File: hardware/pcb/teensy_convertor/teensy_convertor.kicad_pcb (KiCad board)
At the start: 2 copper layers, 76.2 x 101.6 mm, 52 parts, among them SW1 SW_Push, SW2 SW_Push, SW3 SW_Push, SW4 SW_Push, SW5 SW_Push, SW6 SW_Push, SW7 SW_Push, SW8 SW_Push, SW9 SW_Push, U1 Teensy-3.2

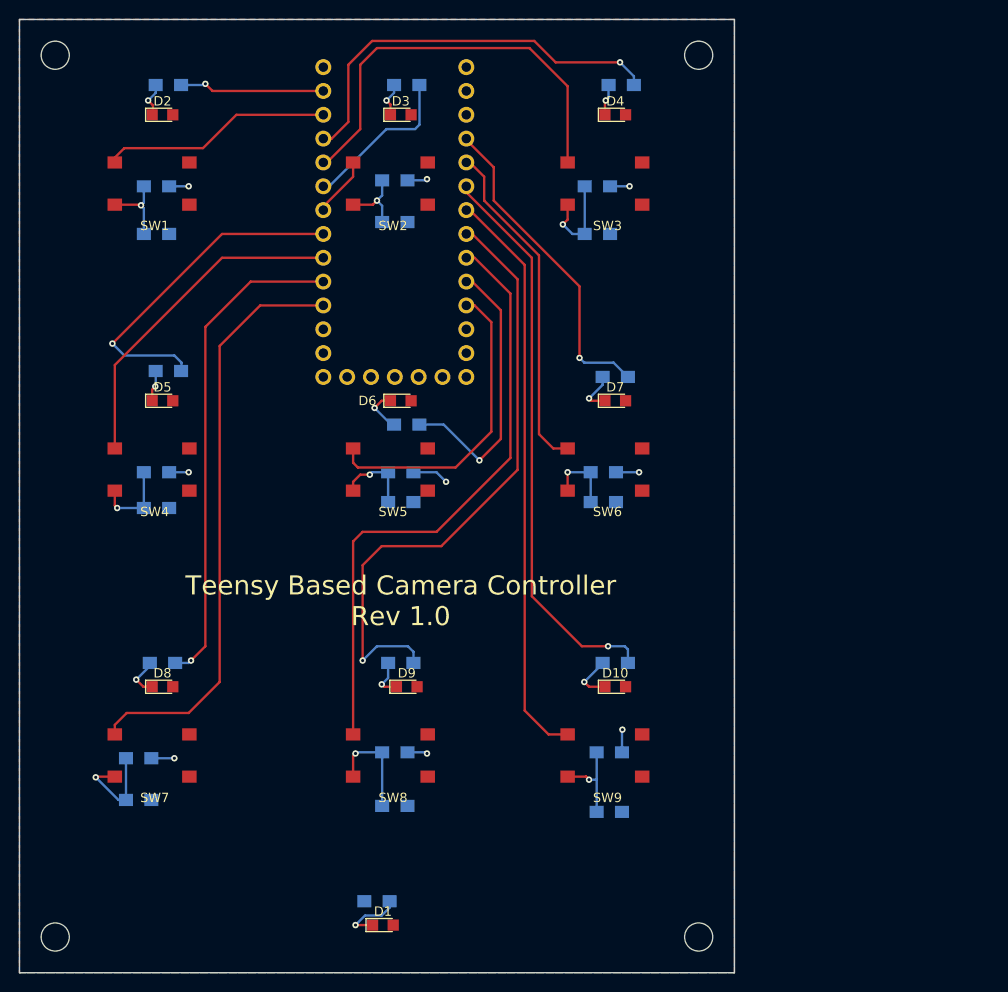
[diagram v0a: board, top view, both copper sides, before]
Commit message: Initial association and import into the layout tool
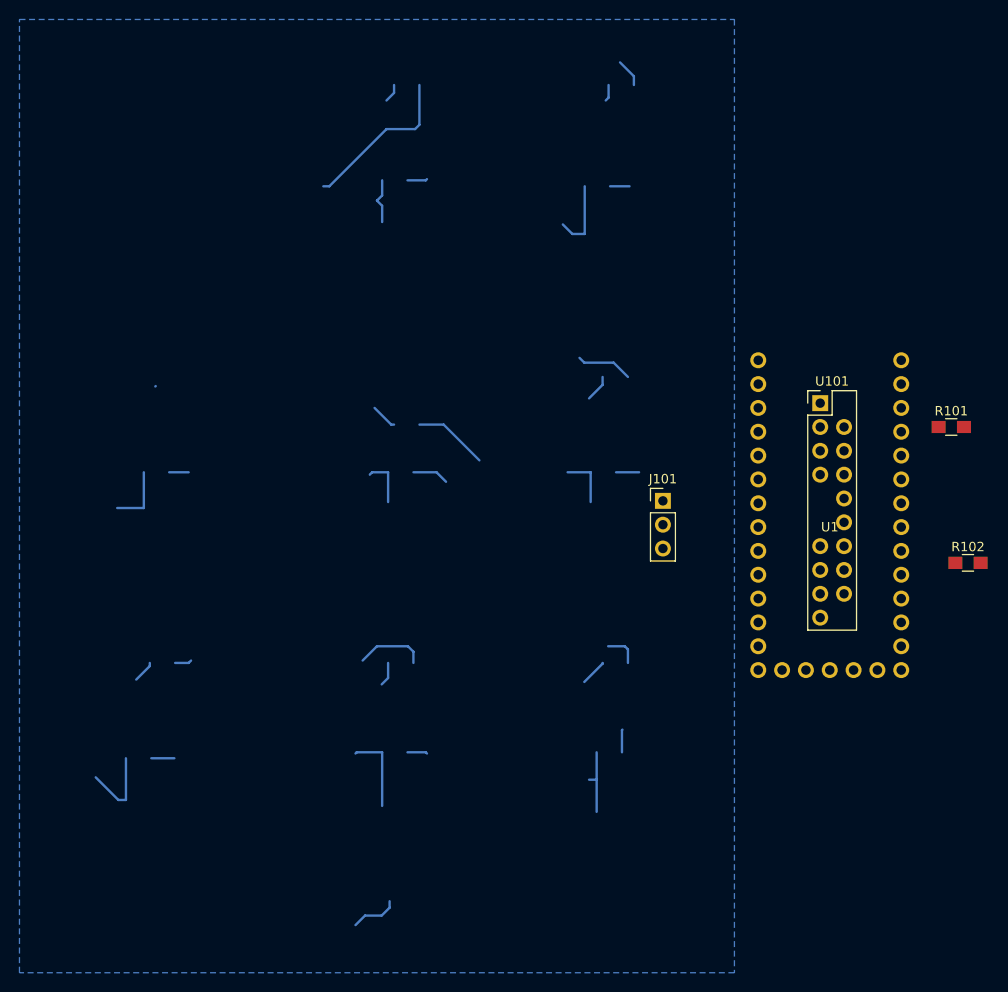
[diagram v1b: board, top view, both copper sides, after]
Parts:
- removed D1, D10, D2, D3, D4, D5, D6, D7, D8, D9: LED, LEDs:LED_0805
- removed R1, R10, R2, R3, R4, R5, R6, R7, R8, R9: 500, Resistors_SMD:R_0805_HandSoldering
- removed R11, R12, R13, R14, R15, R16, R17, R18, R19, R20, R21, R22, R23, R24, R25, R26, R27, R28: 1K, Resistors_SMD:R_0805_HandSoldering
- removed REF** (x4): MountingHole_3mm, Mounting_Holes:MountingHole_3mm
- removed SW1, SW2, SW3, SW4, SW5, SW6, SW7, SW8, SW9: SW_Push, Key:PTS645SK43SMTR92
- added J101: CONN_01X03, Pin_Headers:Pin_Header_Straight_1x03_Pitch2.54mm, F.Cu at (165.1, 91.9)
- added R101: 0, Resistors_SMD:R_0805_HandSoldering, F.Cu at (195.8, 84.1)
- added R102: 0, Resistors_SMD:R_0805_HandSoldering, F.Cu at (197.6, 98.6)
- added U101: MicroC_Header, micro_c_header:MicroC_Header_Pitch2.54mm, F.Cu at (181.9, 81.5)
- U1: footprint Key:Teensy-32 -> teensy_convertor:Teensy-32; moved to F.Cu
- moved U1 55.9 mm to (182.9, 92.2), turned to 0 degrees
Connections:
- U1 pad 0: /LED1 -> /TEENSY_RX
- U1 pad 1: /SW1 -> /TEENSY_TX
- U1 pad 10: Net-(U1-Pad10) -> /SPI_CS
- U1 pad 11: Net-(U1-Pad11) -> /SPI_MOSI
- U1 pad 12: Net-(U1-Pad12) -> /SPI_MISO
- U1 pad 13: Net-(U1-Pad13) -> /SPI_CLK
- U1 pad 14: Net-(U1-Pad14) -> /AIO0
- U1 pad 15: Net-(U1-Pad15) -> /AIO1
- U1 pad 16: /SW5 -> /AIO2
- U1 pad 17: /LED5 -> /AIO3
- U1 pad 18: /SW8 -> /I2C_SDAT
- U1 pad 19: /LED8 -> /I2C_SCLK
- U1 pad 2: /LED3 -> Net-(U1-Pad2)
- U1 pad 20: /SW9 -> Net-(U1-Pad20)
- U1 pad 21: /LED9 -> Net-(U1-Pad21)
- U1 pad 22: /SW6 -> Net-(U1-Pad22)
- U1 pad 23: /LED6 -> Net-(U1-Pad23)
- U1 pad 24: +3V3 -> /3.3V
- U1 pad 26: Net-(U1-Pad26) -> /5.0V
- U1 pad 27: GND -> /GND
- U1 pad 3: /SW3 -> Net-(U1-Pad3)
- U1 pad 4: /LED2 -> Net-(U1-Pad4)
- U1 pad 5: /SW2 -> Net-(U1-Pad5)
- U1 pad 6: /LED4 -> Net-(U1-Pad6)
- U1 pad 7: /SW4 -> Net-(U1-Pad7)
- U1 pad 8: /LED7 -> Net-(U1-Pad8)
- U1 pad 9: /SW7 -> Net-(U1-Pad9)
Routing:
- net (no net): track 0.00 -> 143.9 mm
- net /LED8: track 66.1 -> 0.00 mm, vias 1 -> 0
- net /SW8: track 65.5 -> 0.00 mm
- net /SW7: track 62.7 -> 0.00 mm
- net /SW9: track 61.8 -> 0.00 mm
- net /LED9: track 60.6 -> 0.00 mm, vias 1 -> 0
- net /LED7: track 52.6 -> 0.00 mm, vias 1 -> 0
- net /SW3: track 44.9 -> 0.00 mm
- net /LED3: track 43.5 -> 0.00 mm, vias 1 -> 0
- net /LED4: track 36.4 -> 0.00 mm, vias 1 -> 0
- net /SW6: track 36.1 -> 0.00 mm
- net /SW4: track 35.8 -> 0.00 mm
- net /LED6: track 34.4 -> 0.00 mm, vias 1 -> 0
- net /SW5: track 33.1 -> 0.00 mm
- net /LED5: track 29.9 -> 0.00 mm, vias 1 -> 0
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- removed copper zone on F.Cu, net +3V3
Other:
- board outline removed
- board text removed: "Teensy Based Camera Controller Rev 1.0"

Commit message: Initial layout
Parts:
- added REF**: 1pin, Connect:1pin, F.Cu at (173.5, 75.9)
- U1: moved to B.Cu
- moved J101 20.0 mm to (179.8, 78.5), turned to 90 degrees
- moved R102 19.5 mm to (185.2, 83.6), turned to 270 degrees
- moved R101 7.89 mm to (188.0, 83.6), turned to 90 degrees
- moved U101 3.78 mm to (179.1, 84.1)
- moved U1 0.36 mm to (182.6, 92.5), turned to 180 degrees
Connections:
- U1 pad 30: Net-(U1-Pad30) -> /GND
- U101 pad 7: Net-(U101-Pad7) -> Net-(R101-Pad1)
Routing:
- net (no net): track 143.9 -> 0.00 mm
- net /5.0V: track 0.00 -> 10.9 mm
- net Net-(J101-Pad2): track 0.00 -> 6.96 mm
- net /3.3V: track 0.00 -> 6.40 mm
- net /TEENSY_TX: track 0.00 -> 0.51 mm
- removed copper zone on B.Cu, net GND
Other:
- board outline added: 23.9 x 41.1 mm
- board text added: "3.3V"
- board text added: "5V"

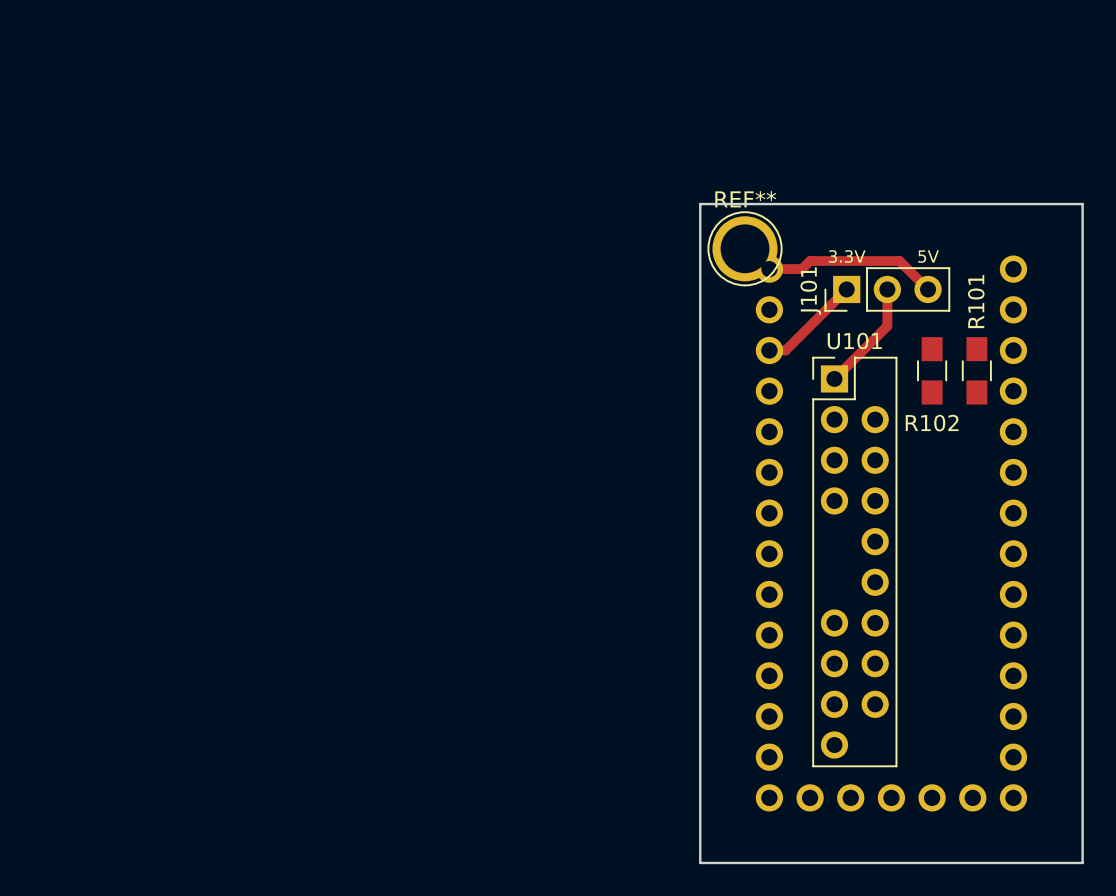
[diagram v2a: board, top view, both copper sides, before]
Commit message: First cut of the complete layout with mounting holes
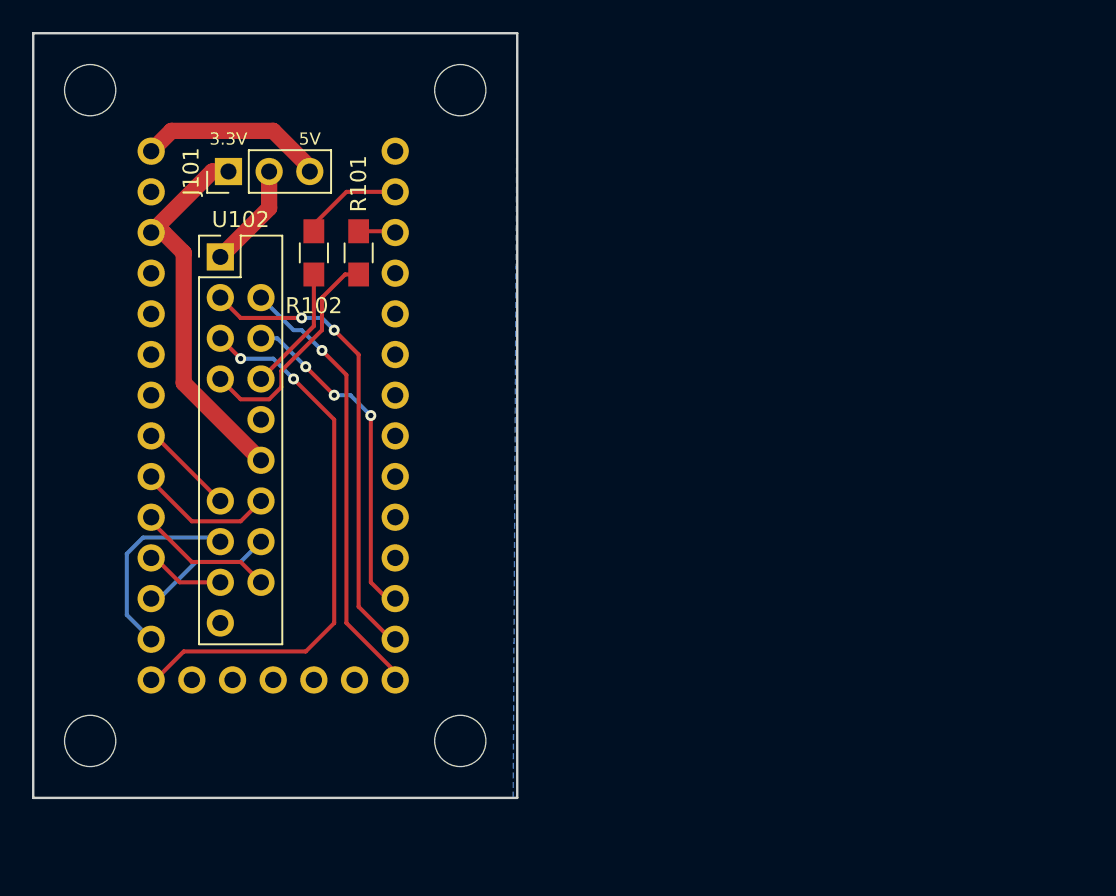
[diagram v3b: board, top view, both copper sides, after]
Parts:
- removed the REF** at (173.5, 75.9)
- removed U101: MicroC_Header, micro_c_header:MicroC_Header_Pitch2.54mm
- added REF**: MountingHole_3.2mm_M3, Mounting_Holes:MountingHole_3.2mm_M3, F.Cu at (155.7, 106.7)
- added REF**: MountingHole_3.2mm_M3, Mounting_Holes:MountingHole_3.2mm_M3, F.Cu at (132.6, 106.7)
- added REF**: MountingHole_3.2mm_M3, Mounting_Holes:MountingHole_3.2mm_M3, F.Cu at (132.6, 66.0)
- added REF**: MountingHole_3.2mm_M3, Mounting_Holes:MountingHole_3.2mm_M3, F.Cu at (155.7, 66.0)
- added U102: MicroC_Header, micro_c_header:MicroC_Header_Pitch2.54mm, F.Cu at (140.7, 76.5)
- moved J101 39.3 mm to (141.2, 71.1)
- moved R101 39.3 mm to (149.4, 76.2)
- moved R102 39.3 mm to (146.6, 76.2)
- moved U1 39.3 mm to (144.0, 85.1)
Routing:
- net /SPI_CLK: track 0.00 -> 34.8 mm, vias 0 -> 2
- net /SPI_MOSI: track 0.00 -> 29.0 mm, vias 0 -> 2
- net /SPI_MISO: track 0.00 -> 27.6 mm, vias 0 -> 1
- net /SPI_CS: track 0.00 -> 21.5 mm, vias 0 -> 3
- net /3.3V: track 6.40 -> 23.9 mm
- net Net-(R101-Pad1): track 0.00 -> 14.2 mm
- net /AIO0: track 0.00 -> 12.3 mm
- net /AIO3: track 0.00 -> 8.69 mm
- net /I2C_SDAT: track 0.00 -> 8.69 mm
- net /AIO1: track 0.00 -> 8.33 mm
- net Net-(R102-Pad2): track 0.00 -> 7.89 mm
- net /TEENSY_RX: track 0.00 -> 6.35 mm
- net /I2C_SCLK: track 0.00 -> 6.00 mm
- net /AIO2: track 0.00 -> 4.95 mm
- net /TEENSY_TX: track 0.51 -> 2.32 mm
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- added copper zone on B.Cu, net /GND
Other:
- board size 23.9 x 41.1 mm -> 30.2 x 47.8 mm

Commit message: final layout
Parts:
- removed U1: Teensy-3.2, teensy_convertor:Teensy-32
- added U101: Teensy-3.2, teensy_convertor:Teensy-32, B.Cu at (144.0, 85.1)
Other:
- board text added: "MicroController Header"
- board text added: "Teensy uC"
